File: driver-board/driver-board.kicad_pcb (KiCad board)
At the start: 2 copper layers, 85 x 58 mm, 57 parts, among them J1 MCP4725, J2 Conn_Coaxial, J3 MCP4725, J4 Conn_Coaxial, SW1 RST, SW2 BIAS ON/OF, U1 Pico, U2 MIC5317, U3 TSV358, U4 TSV358, U5 TCBT-2R5G, U6 LM2904, U7 LT3462A

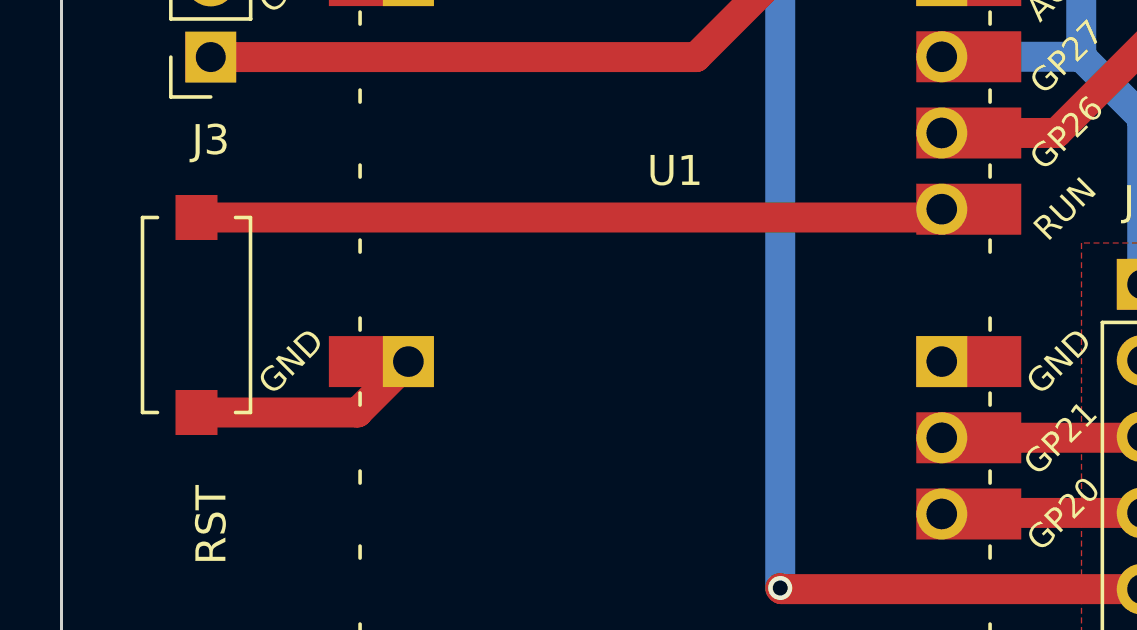
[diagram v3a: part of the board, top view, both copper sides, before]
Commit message: updated rst button fp
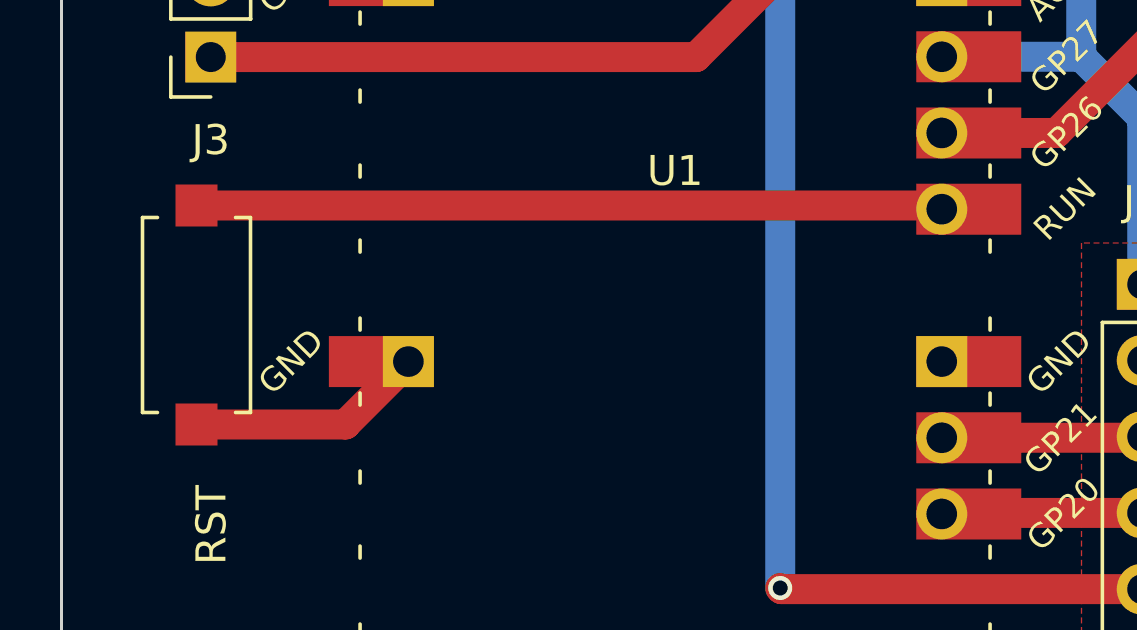
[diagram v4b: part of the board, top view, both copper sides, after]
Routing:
- net GND: track 48.3 -> 56.6 mm
- net Net-(C14-Pad2): track 8.13 -> 0.00 mm
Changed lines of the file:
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@@
       (effects (font (size 1 1) (thickness 0.15)))
     )
+    (fp_line (start 6.5 1.8) (end 0 1.8) (layer "F.SilkS") (width 0.12))
     (fp_line (start 0 -1.3) (end 0 -1.8) (layer "F.SilkS") (width 0.12))
+    (fp_line (start 6.5 -1.3) (end 6.5 -1.8) (layer "F.SilkS") (width 0.12))
     (fp_line (start 0 1.8) (end 0 1.3) (layer "F.SilkS") (width 0.12))
+    (fp_line (start 6.5 1.8) (end 6.5 1.3) (layer "F.SilkS") (width 0.12))
     (fp_line (start 0 -1.8) (end 6.5 -1.8) (layer "F.SilkS") (width 0.12))
-    (fp_line (start 6.5 -1.3) (end 6.5 -1.8) (layer "F.SilkS") (width 0.12))
-    (fp_line (start 6.5 1.8) (end 0 1.8) (layer "F.SilkS") (width 0.12))
-    (fp_line (start 6.5 1.8) (end 6.5 1.3) (layer "F.SilkS") (width 0.12))
-    (pad "1" smd rect (at 0 0 270) (size 1.5 1.4) (layers "F.Cu" "F.Paste" "F.Mask")
+    (pad "1" smd rect (at -0.4 0 270) (size 1.4 1.4) (layers "F.Cu" "F.Paste" "F.Mask")
       (net 5 "Net-(SW1-Pad1)") (pinfunction "1") (pintype "passive"))
-    (pad "2" smd rect (at 6.5 0 270) (size 1.5 1.4) (layers "F.Cu" "F.Paste" "F.Mask")
+    (pad "2" smd rect (at 6.9 0 270) (size 1.4 1.4) (layers "F.Cu" "F.Paste" "F.Mask")
       (net 2 "GND") (pinfunction "2") (pintype "passive"))
   )
@@
   (segment (start 123 114) (end 123 115.9625) (width 0.5) (layer "F.Cu") (net 2))
   (segment (start 103.6625 76.3) (end 104.0625 75.9) (width 0.5) (layer "F.Cu") (net 2))
-  (segment (start 67.865 107.25) (end 69.5625 105.5525) (width 1) (layer "F.Cu") (net 2))
+  (segment (start 67.465 107.65) (end 69.5625 105.5525) (width 1) (layer "F.Cu") (net 2))
+  (segment (start 101.1375 119.5) (end 100.541796 119.5) (width 0.55) (layer "F.Cu") (net 2))
   (segment (start 140.05 115.05) (end 140.05 117.3) (width 1) (layer "F.Cu") (net 2))
+  (segment (start 100.541796 119.5) (end 100 118.958204) (width 0.55) (layer "F.Cu") (net 2))
   (segment (start 103.2775 87.9025) (end 105.3975 87.9025) (width 0.5) (layer "F.Cu") (net 2))
   (segment (start 116.2 86) (end 114.0625 86) (width 1) (layer "F.Cu") (net 2))
@@
   (segment (start 100.921088 102.411088) (end 100.921088 100.941088) (width 0.5) (layer "F.Cu") (net 2))
   (segment (start 130.8 102.6) (end 133.5 102.6) (width 1) (layer "F.Cu") (net 2))
+  (segment (start 101.1375 119.5) (end 104.9875 119.5) (width 0.55) (layer "F.Cu") (net 2))
   (segment (start 106.4 80.1) (end 104.6 80.1) (width 1) (layer "F.Cu") (net 2))
+  (segment (start 62.5 107.65) (end 67.465 107.65) (width 1) (layer "F.Cu") (net 2))
   (segment (start 105.1 117.7) (end 105.1 116) (width 1) (layer "F.Cu") (net 2))
   (segment (start 97.4 109) (end 98.9625 109) (width 0.55) (layer "F.Cu") (net 2))
   (segment (start 115.3 108) (end 115.275 107.975) (width 0.4) (layer "F.Cu") (net 2))
-  (segment (start 62.5 107.25) (end 67.865 107.25) (width 1) (layer "F.Cu") (net 2))
   (segment (start 118.8625 106.675) (end 117.025 106.675) (width 0.4) (layer "F.Cu") (net 2))
   (segment (start 114.0375 78.5) (end 116.8 78.5) (width 1) (layer "F.Cu") (net 2))
   (segment (start 114 75) (end 116.8 75) (width 1) (layer "F.Cu") (net 2))
   (segment (start 99.9 89.1) (end 99.9 88.9) (width 0.55) (layer "F.Cu") (net 2))
+  (segment (start 100 118.958204) (end 100 116.0375) (width 0.55) (layer "F.Cu") (net 2))
   (segment (start 123.1 103.0625) (end 123.1 101.5) (width 1) (layer "F.Cu") (net 2))
   (segment (start 103.683588 93.3) (end 103.683588 91.748588) (width 0.5) (layer "F.Cu") (net 2))
@@
   (segment (start 94.024999 97.524999) (end 94.024999 102.9775) (width 1) (layer "B.Cu") (net 4))
   (segment (start 91.9925 95.3925) (end 91.9925 85.4075) (width 1) (layer "B.Cu") (net 4))
-  (segment (start 62.5 100.75) (end 87.065 100.75) (width 1) (layer "F.Cu") (net 5))
+  (segment (start 87.3425 100.4725) (end 87.22 100.35) (width 1) (layer "F.Cu") (net 5))
+  (segment (start 87.22 100.35) (end 62.5 100.35) (width 1) (layer "F.Cu") (net 5))
   (segment (start 107.3 82) (end 118.4 82) (width 1) (layer "F.Cu") (net 6))
   (segment (start 105.4 83.9) (end 105.4025 83.9025) (width 0.5) (layer "F.Cu") (net 6))
@@
   (segment (start 62.975 87.7825) (end 69.5525 87.7825) (width 0.5) (layer "F.Cu") (net 27))
   (segment (start 62.975 90.3225) (end 69.5525 90.3225) (width 0.5) (layer "F.Cu") (net 28))
-  (segment (start 101.1375 119.5) (end 100.541796 119.5) (width 0.55) (layer "F.Cu") (net 30))
-  (segment (start 100.541796 119.5) (end 100 118.958204) (width 0.55) (layer "F.Cu") (net 30))
-  (segment (start 101.1375 119.5) (end 104.9875 119.5) (width 0.55) (layer "F.Cu") (net 30))
-  (segment (start 100 118.958204) (end 100 116.0375) (width 0.55) (layer "F.Cu") (net 30))
   (segment (start 118.8625 107.6375) (end 120.1625 107.6375) (width 0.5) (layer "F.Cu") (net 34))
   (segment (start 118.8625 107.6375) (end 118.8625 107.37452) (width 0.5) (layer "F.Cu") (net 34))

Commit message: Cleanup, trying simpler board with no RF switch
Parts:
- removed C18: 0.1u, Capacitor_SMD:C_0805_2012Metric_Pad1.18x1.45mm_HandSolder
- removed C19: 0.01u, Capacitor_SMD:C_0805_2012Metric_Pad1.18x1.45mm_HandSolder
- removed JP2: SolderJumper_2_Bridged, Jumper:SolderJumper-2_P1.3mm_Bridged_Pad1.0x1.5mm
- removed LD1: D_Laser_Photo_NType, Package_TO_SOT_THT:TO-46-3
- removed R4: 470k, Resistor_SMD:R_0805_2012Metric_Pad1.20x1.40mm_HandSolder
- removed R5: 18k, Resistor_SMD:R_0805_2012Metric_Pad1.20x1.40mm_HandSolder
- removed R6, R8: 0, Resistor_SMD:R_0805_2012Metric_Pad1.20x1.40mm_HandSolder
- removed REF** (x3): MountingHole_3.2mm_M3, MountingHole:MountingHole_3.2mm_M3
- removed RV2: 100K, lib:PT15-RV15
- removed TP3, TP4, TP5, TP6, TP7: TestPoint, TestPoint:TestPoint_Pad_D1.5mm
- added J5: Conn_Coaxial, lib:CONSMA020.062-G, F.Cu at (87.7, 91.3)
- added RV1: 100K, lib:PT15-RV15, F.Cu at (128.5, 161.5)
- added U8: VCSEL, lib:VP-SMD-5050, F.Cu at (124.5, 68.0)
- C10: value 0.01u -> 0.1u
- C11: value 0.1u -> 0.01u
- C12: value 100u -> 0.1u; footprint Capacitor_THT:CP_Radial_D10.0mm_P3.50mm -> Capacitor_SMD:C_0805_2012Metric_Pad1.18x1.45mm_HandSolder
- C13, C16: value 1u -> 0.01u
- C14: value 1u -> 0.1u
- C15: value 22p -> 100u; footprint Capacitor_SMD:C_0805_2012Metric_Pad1.18x1.45mm_HandSolder -> Capacitor_THT:CP_Radial_D10.0mm_P3.50mm
- C17: value 1u -> 0.01u; moved to F.Cu
- C3, C4: value 0.1u -> 1u
- C5: value 0.01u -> 22p; moved to F.Cu
- C6: value C_Small -> 0
- C7: value C_Small -> 1u
- C9: value 0 -> 1u
- FID1, U5: moved to F.Cu
- J1: value MCP4725 -> Conn_01x04_Male; footprint Connector_PinSocket_2.54mm:PinSocket_1x06_P2.54mm_Vertical -> Connector_PinHeader_2.54mm:PinHeader_1x04_P2.54mm_Vertical
- J2: value Conn_Coaxial -> MCP4725; footprint lib:CONSMA020.062-G -> Connector_PinSocket_2.54mm:PinSocket_1x06_P2.54mm_Vertical; moved to F.Cu
- J3: value MCP4725 -> Conn_Coaxial; footprint Connector_PinSocket_2.54mm:PinSocket_1x06_P2.54mm_Vertical -> lib:CONSMA020.062-G
- JP1: value SolderJumper_2_Open -> SolderJumper_2_Bridged
- R1: value 10 -> 470k
- R2: value R -> 18k
- R3: value 1k -> 10
- R7: value 0 -> 1k
- SW1: value RST -> BIAS ON/OF; footprint lib:PTS636 SM43J -> lib:JS202011SCQN
- U1: value Pico -> LT3462A; footprint lib:RPi_Pico_minimal -> lib:LT3462A
- U3: value TSV358 -> LM2904; footprint lib:SOIC-8-1EP_3.9x4.9mm_P1.27mm_EP2.29x3mm -> Package_SO:TSSOP-8_4.4x3mm_P0.65mm
- U6: value LM2904 -> TCBT-2R5G; footprint Package_SO:TSSOP-8_4.4x3mm_P0.65mm -> lib:TCBT
- U7: value LT3462A -> VCSEL; footprint lib:LT3462A -> lib:VP-SMD-5050
- moved U1 164.0 mm to (240.3, 125.5), turned to 180 degrees
- moved C1 143.6 mm to (238.0, 122.0), turned to 180 degrees
- moved L1 139.2 mm to (238.5, 119.0), turned to 0 degrees
- moved J2 138.6 mm to (4.72, 138.1), turned to 180 degrees
- moved C7 133.3 mm to (244.0, 123.5), turned to 0 degrees
- moved R2 133.0 mm to (239.4, 127.8), turned to 0 degrees
- moved R1 132.1 mm to (243.0, 127.0), turned to -90 degrees
- moved C4 130.9 mm to (235.4, 99.7)
- moved C8 130.7 mm to (235.4, 106.7)
- moved L2 130.1 mm to (235.0, 126.5)
- moved U2 130.0 mm to (235.5, 95.0), turned to -90 degrees
- moved C5 125.9 mm to (245.0, 127.0)
- moved C3 125.8 mm to (234.4, 121.5)
- moved C2 123.5 mm to (235.4, 90.7)
- moved C6 119.0 mm to (235.4, 103.2), turned to 180 degrees
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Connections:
- C1 pad 1: 5V -> GND
- C1 pad 2: GND -> 5V
- C10 pad 1: Net-(C10-Pad1) -> GND
- C10 pad 2: GND -> +3.3VA
- C11 pad 2: SiPM Bias -> +3.3VA
- C12 pad 1: GND -> +3.3VA
- C12 pad 2: SiPM Bias -> GND
- C13 pad 1: GND -> Net-(C13-Pad1)
- C13 pad 2: 5V -> GND
- C14 pad 1: Net-(C14-Pad1) -> GND
- C14 pad 2: Net-(C14-Pad2) -> SiPM Bias
- C15 pad 1: Net-(C15-Pad1) -> GND
- C15 pad 2: -33V -> SiPM Bias
- C16 pad 2: -33V -> DC_LD1
- C17 pad 2: A3V3 -> DC_LD2
- C2 pad 1: A3V3 -> 5V
- C3 pad 1: A3V3 -> Net-(C3-Pad1)
- C3 pad 2: GND -> Net-(C3-Pad2)
- C4 pad 1: A3V3 -> +3.3VA
- C5 pad 1: GND -> Net-(C5-Pad1)
- C5 pad 2: Net-(C5-Pad2) -> -33V
- C6 pad 1: PD -> +3.3VA
- C6 pad 2: TIA_OUT -> GND
- C7 pad 1: PD -> GND
- C7 pad 2: TIA_OUT -> -33V
- C8 pad 1: A3V3 -> +3.3VA
- C9 pad 1: A3V3 -> GND
- C9 pad 2: GND -> +3.3VA
- J1 pad 1: DAC_OUT_I_SRC -> 5V
- J1 pad 2: GND -> SDA0
- J1 pad 4: SDA0 -> GND
- J2 pad 1: Net-(J2-Pad1) -> DAC_OUT_I_SRC
- J3 pad 1: DAC_OUT_TIA -> SiPM Bias
- J4 pad 1: SiPM Bias -> Net-(J4-Pad1)
- JP1 pad 1: DAC_OUT_TIA -> Net-(JP1-Pad1)
- L1 pad 2: Net-(C14-Pad1) -> Net-(C3-Pad1)
- L2 pad 1: Net-(C14-Pad2) -> Net-(C3-Pad2)
- R1 pad 1: Net-(JP2-Pad1) -> Net-(C5-Pad1)
- R1 pad 2: Net-(R1-Pad2) -> -33V
- R2 pad 1: PD -> Net-(R2-Pad1)
- R2 pad 2: TIA_OUT -> Net-(C5-Pad1)
- R3 pad 1: SiPM Bias -> Net-(JP1-Pad1)
- R3 pad 2: Net-(C10-Pad1) -> Net-(R3-Pad2)
- R7 pad 1: Net-(R7-Pad1) -> SiPM Bias
- R7 pad 2: Net-(R7-Pad2) -> Net-(C13-Pad1)
- RN1 pad 1: Net-(R1-Pad2) -> Net-(R3-Pad2)
- RN1 pad 2: DAC_OUT_I_SRC -> GND
- RN1 pad 3: Net-(RN1-Pad3) -> DAC_OUT_I_SRC
- RN1 pad 4: GND -> Net-(U4-Pad6)
- RN1 pad 5: Net-(RN1-Pad5) -> Net-(RN1-Pad6)
- RN1 pad 6: Net-(RN1-Pad5) -> Net-(RN1-Pad6)
- SW1 pad 1: Net-(SW1-Pad1) -> Net-(RV1-Pad2)
- SW1 pad 2: GND -> Net-(C13-Pad1)
- SW2 pad 1: Net-(RV2-Pad2) -> DC_LD1
- SW2 pad 2: Net-(C10-Pad1) -> Net-(JP1-Pad2)
- SW2 pad 3: GND -> DC_LD2
- U1 pad 6: SDA1 -> unconnected-(U1-Pad6)
- U1 pad 7: SCL1 -> Net-(C3-Pad2)
- U1 pad 8: GND -> Net-(R2-Pad1)
- U2 pad 5: A3V3 -> +3.3VA
- U3 pad 1: Net-(R1-Pad2) -> Net-(C13-Pad1)
- U3 pad 2: Net-(RN1-Pad7) -> Net-(C13-Pad1)
- U3 pad 3: Net-(RN1-Pad5) -> GND
- U3 pad 4: GND -> -33V
- U3 pad 5: Net-(JP2-Pad1) -> unconnected-(U3-Pad5)
- U3 pad 6: Net-(RN1-Pad3) -> unconnected-(U3-Pad6)
- U3 pad 7: Net-(RN1-Pad3) -> unconnected-(U3-Pad7)
- U3 pad 8: A3V3 -> GND
- U4 pad 1: unconnected-(U4-Pad1) -> Net-(R3-Pad2)
- U4 pad 2: unconnected-(U4-Pad2) -> Net-(RN1-Pad7)
- U4 pad 3: unconnected-(U4-Pad3) -> Net-(RN1-Pad6)
- U4 pad 5: Net-(JP1-Pad2) -> Net-(JP1-Pad1)
- U4 pad 6: PD -> Net-(U4-Pad6)
- U4 pad 7: TIA_OUT -> Net-(U4-Pad6)
- U4 pad 8: A3V3 -> +3.3VA
- U5 pad 1: Net-(C5-Pad2) -> DC_LD1
- U5 pad 3: LD_LOW -> Net-(U5-Pad3)
- U5 pad 4: Net-(J2-Pad1) -> Net-(J4-Pad1)
- U6 pad 1: Net-(C10-Pad1) -> DC_LD2
- U6 pad 2: Net-(C10-Pad1) -> unconnected-(U6-Pad2)
- U6 pad 3: GND -> Net-(U6-Pad3)
- U6 pad 4: -33V -> Net-(J5-Pad1)
- U7 pad 1: Net-(C15-Pad1) -> GND
- U7 pad 2: GND -> unconnected-(U7-Pad2)
- U7 pad 3: GND -> unconnected-(U7-Pad3)
- U7 pad 4: Net-(C14-Pad1) -> unconnected-(U7-Pad4)
- U7 pad 5: 5V -> unconnected-(U7-Pad5)
- U7 pad 6: unconnected-(U7-Pad6) -> Net-(U5-Pad3)
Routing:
- net 3V3: track 64.3 -> 0.00 mm, vias 2 -> 0
- net A3V3: track 61.8 -> 0.00 mm, vias 4 -> 0
- net GND: track 56.6 -> 7.53 mm, vias 55 -> 0
- net DAC_OUT_TIA: track 48.6 -> 0.00 mm, vias 2 -> 0
- net PD: track 42.6 -> 0.00 mm
- net TIA_OUT: track 34.5 -> 0.00 mm
- net DAC_OUT_I_SRC: track 34.7 -> 3.21 mm, vias 1 -> 0
- net Net-(SW1-Pad1): track 24.9 -> 0.00 mm
- net Net-(C10-Pad1): track 23.3 -> 0.00 mm
- net SiPM Bias: track 25.6 -> 2.77 mm
- net Net-(RV2-Pad2): track 21.3 -> 0.00 mm, vias 2 -> 0
- net -33V: track 0.00 -> 19.9 mm
- net Net-(R1-Pad2): track 19.8 -> 0.00 mm
- net Net-(RN1-Pad3): track 19.4 -> 0.00 mm
- net Net-(R3-Pad2): track 0.00 -> 17.2 mm
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- added copper zone on F.Cu, net Net-(C3-Pad1)
- added copper zone on F.Cu, net Net-(C3-Pad2)
- added copper zone on F.Cu, net Net-(C5-Pad1)
- added copper zone on F.Cu, net Net-(R2-Pad1)
- removed copper zone on F.Cu, net -33V
- removed copper zone on F.Cu, net A3V3
- removed copper zone on B.Cu, net GND
- removed copper zone on F.Cu, net GND
- removed copper zone on F.Cu, net Net-(C14-Pad1)
- removed copper zone on F.Cu, net Net-(C15-Pad1)
- removed copper zone on F.Cu, net Net-(R5-Pad1)
- removed copper zone on F.Cu, net SiPM Bias
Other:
- board outline removed
- board text removed: "-V Bias"
- board text removed: "BIAS ON/OFF"
- board text removed: "Boost Converter"
- board text removed: "Current Source"
- board text removed: "DAC Current Source"
- board text removed: "FD-fNIRS v1 rohitrathnam.n@gmail.com mendi.io"
- board text removed: "RST"
- board text removed: "Raspberry Pi Pico"
- board text removed: "TIA"

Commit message: DRC passing
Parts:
- removed C10: 0.1u, Capacitor_SMD:C_0805_2012Metric_Pad1.18x1.45mm_HandSolder
- removed C11: 0.01u, Capacitor_SMD:C_0805_2012Metric_Pad1.18x1.45mm_HandSolder
- removed C9: 1u, Capacitor_SMD:C_0805_2012Metric_Pad1.18x1.45mm_HandSolder
- added R4: 0, Resistor_SMD:R_0805_2012Metric_Pad1.20x1.40mm_HandSolder, B.Cu at (205.6, 103.5)
- added R5: 0, Resistor_SMD:R_0805_2012Metric_Pad1.20x1.40mm_HandSolder, B.Cu at (209.4, 103.5)
- added R6: 0, Resistor_SMD:R_0805_2012Metric_Pad1.20x1.40mm_HandSolder, B.Cu at (201.8, 103.5)
- J1: value Conn_01x04_Male -> Conn_01x05_Male; footprint Connector_PinHeader_2.54mm:PinHeader_1x04_P2.54mm_Vertical -> Connector_PinHeader_2.54mm:PinHeader_1x05_P2.54mm_Vertical
- moved RN1 159.9 mm to (185.0, 98.1), turned to -90 degrees
- moved TP1 159.6 mm to (180.7, 96.2), turned to 90 degrees
- moved J2 159.0 mm to (157.1, 92.6), turned to 0 degrees
- moved SW2 155.3 mm to (185.4, 91.4), turned to 90 degrees
- moved C12 152.1 mm to (187.4, 106.2), turned to 90 degrees
- moved U4 150.6 mm to (183.2, 104.7), turned to -90 degrees
- moved R3 145.7 mm to (185.6, 110.5), turned to 0 degrees
- moved JP1 139.7 mm to (178.6, 106.7), turned to 90 degrees
- moved J3 132.8 mm to (214.5, 74.0)
- moved J4 126.7 mm to (222.7, 111.9)
- moved U7 125.1 mm to (231.8, 102.8), turned to -90 degrees
- moved C15 121.4 mm to (193.4, 81.9)
- moved J5 119.6 mm to (205.6, 111.9)
- moved U8 111.1 mm to (231.8, 96.8), turned to -90 degrees
- moved C14 109.6 mm to (183.7, 79.7), turned to -90 degrees
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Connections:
- J1 pad 2: SDA0 -> 3V3
- J1 pad 3: SCL0 -> SDA0
- J1 pad 4: GND -> SCL0
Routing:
- net 5V: track 4.43 -> 63.5 mm, vias 1 -> 2
- net DC_LD1: track 0.00 -> 44.4 mm, vias 0 -> 2
- net SiPM Bias: track 2.77 -> 38.2 mm
- net Net-(C13-Pad1): track 6.06 -> 39.0 mm
- net DAC_OUT_I_SRC: track 3.21 -> 31.3 mm, vias 0 -> 2
- net DC_LD2: track 0.00 -> 26.6 mm
- net -33V: track 19.9 -> 45.5 mm, vias 0 -> 2
- net Net-(U6-Pad3): track 0.00 -> 23.7 mm
- net Net-(JP1-Pad2): track 0.00 -> 21.5 mm
- net +3.3VA: track 2.25 -> 20.2 mm, vias 0 -> 2
- net Net-(J5-Pad1): track 0.00 -> 16.6 mm
- net Net-(RV1-Pad2): track 0.00 -> 12.0 mm
- net Net-(U5-Pad3): track 0.00 -> 9.13 mm
- net Net-(J4-Pad1): track 0.00 -> 8.17 mm
- net GND: track 7.53 -> 15.4 mm, vias 0 -> 3
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- added copper zone on F.Cu, net -33V
- added copper zone on B.Cu, net GND
- added copper zone on F.Cu, net GND
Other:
- board outline added: 90 x 45.1 mm

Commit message: minor fixes
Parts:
- added FID1: Logo, lib:mendi-logo-plain, B.Cu at (124.2, 72.0)
- moved JP1 47.6 mm to (131.0, 104.5)
- moved R6 47.6 mm to (154.2, 101.3)
- moved RN1 47.6 mm to (137.4, 95.9)
- moved C13 47.6 mm to (127.8, 86.0)
- moved J2 47.6 mm to (109.5, 90.5)
- moved RV1 47.6 mm to (117.9, 77.0)
- moved SW1 47.6 mm to (106.5, 82.3)
- moved C1 47.6 mm to (122.2, 101.0)
- moved C12 47.6 mm to (139.8, 104.0)
- moved C14 47.6 mm to (136.1, 77.5)
- moved C15 47.6 mm to (145.8, 79.8)
- moved C16 47.6 mm to (169.0, 100.2)
- moved C17 47.6 mm to (159.1, 86.3)
- moved C2 47.6 mm to (145.2, 108.4)
- moved C3 47.6 mm to (125.8, 101.5)
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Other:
- board size 90 x 45.1 mm -> 90 x 45 mm
- board text added: "FD-fNIRS v2 rohitrathnam.n@gmail.com"

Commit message: generated gerbers
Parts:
- moved J3 8.10 mm to (175.0, 71.8)
- moved C1 0.10 mm to (122.2, 101.0)
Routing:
- net SiPM Bias: track 38.2 -> 46.0 mm
- net -33V: track 45.5 -> 44.4 mm
- net GND: track 15.4 -> 15.5 mm, vias 3 -> 61
